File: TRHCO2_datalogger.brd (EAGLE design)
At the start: 57.7 x 51.3 mm, 31 parts, among them J3 USB-MICROB, U1 ATMEGA328P-MU, U7 SHT31/35, U8 MCP1703/3.3V, Y1 16MHZ

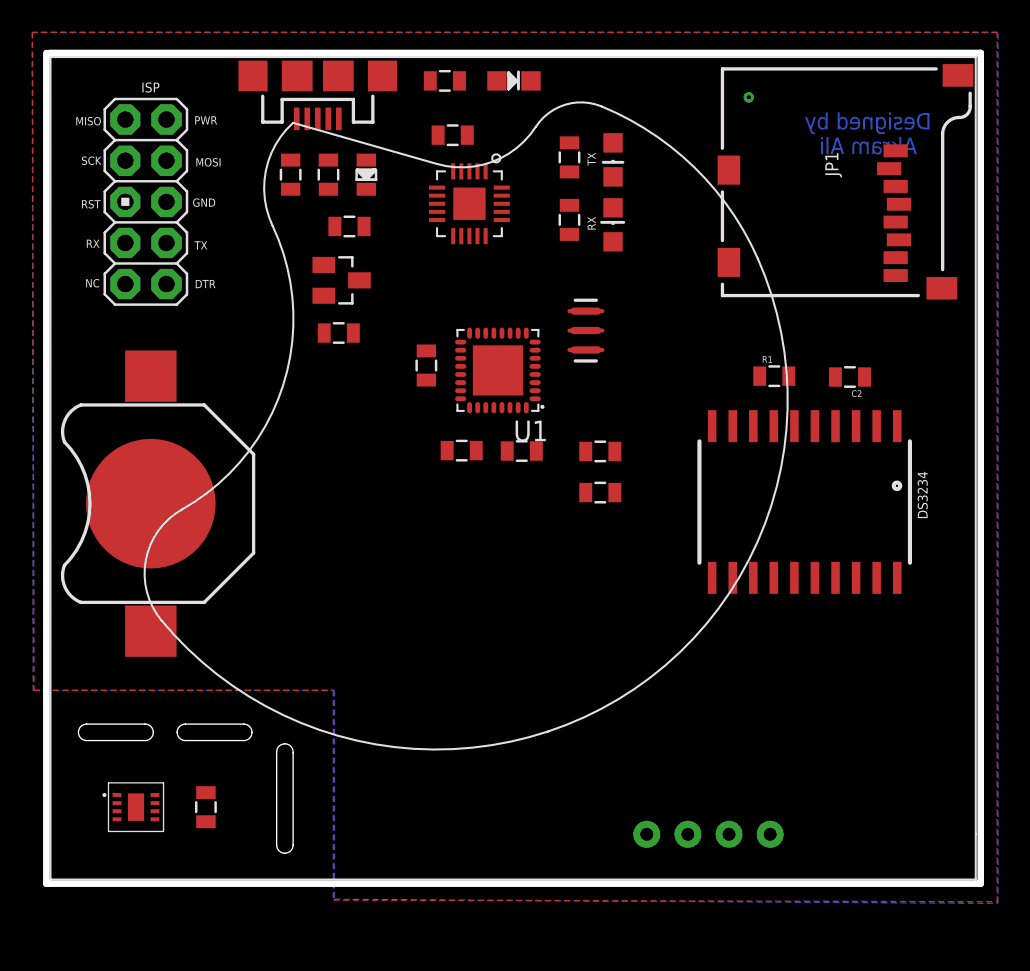
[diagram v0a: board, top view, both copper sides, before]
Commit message: Completed v0.1 design
Routed all traces
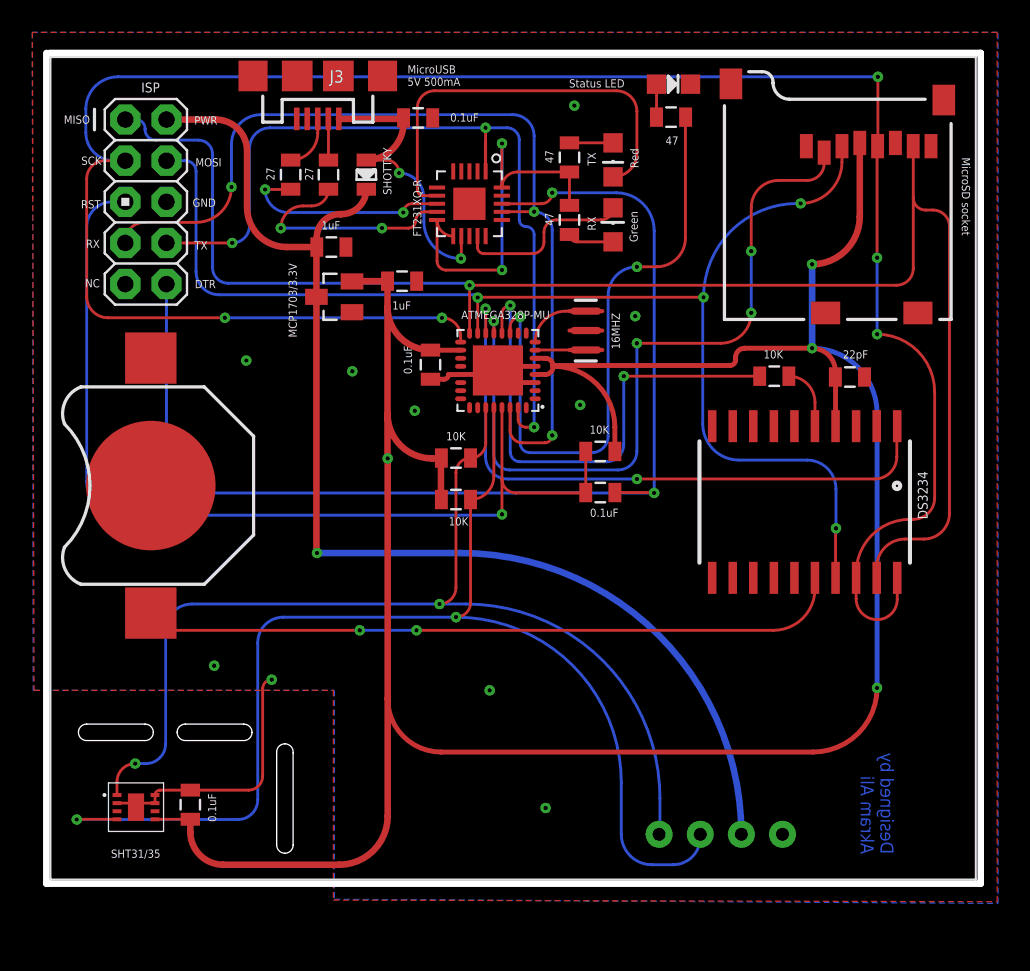
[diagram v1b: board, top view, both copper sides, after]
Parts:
- J3: value USB-MICROB -> MicroUSB (5V)
- JP1: value USD-SOCKETNEW -> MicroSD socket
- moved JP1 14.2 mm to (56.6, 38.0), turned to 0 degrees
- moved R4 14.1 mm to (39.3, 50.5), turned to 180 degrees
- moved LED1 9.86 mm to (39.4, 52.5)
- moved C6 5.05 mm to (22.7, 40.4)
- moved R6 5.05 mm to (26.0, 26.9), turned to 180 degrees
- moved C11 2.39 mm to (23.7, 50.4)
- moved C1 1.69 mm to (18.3, 42.5), turned to 0 degrees
- moved BAT1 1.12 mm to (7.16, 27.7)
- moved U8 1.11 mm to (18.5, 39.4), turned to 90 degrees
- moved C4 0.98 mm to (9.60, 8.03)
- moved R5 0.58 mm to (26.0, 29.4)
- moved C15 0.26 mm to (24.4, 35.2)
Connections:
- net D4 renamed N$2
- removed net N$1 (its old number): U1.12
- net D8: now also U1.12
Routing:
- net VCC: track 0.00 -> 166.4 mm, vias 0 -> 4
- net SCK: track 0.00 -> 129.7 mm, vias 0 -> 5
- net MISO: track 0.00 -> 95.3 mm, vias 0 -> 1
- net MOSI: track 0.00 -> 78.7 mm, vias 0 -> 4
- net SCL: track 0.00 -> 74.9 mm, vias 0 -> 2
- net PWR: track 0.00 -> 71.8 mm, vias 0 -> 1
- net DTR: track 0.00 -> 71.3 mm, vias 0 -> 2
- net SDA: track 0.00 -> 64.2 mm, vias 0 -> 2
- net RESET: track 0.00 -> 60.0 mm, vias 0 -> 1
- net RX: track 0.00 -> 56.1 mm, vias 0 -> 3
- net TX: track 0.00 -> 52.4 mm, vias 0 -> 3
- net D9: track 0.00 -> 46.0 mm, vias 0 -> 4
- net N$8: track 0.00 -> 44.3 mm, vias 0 -> 2
- net SS: track 0.00 -> 39.1 mm, vias 0 -> 2
- net N$1: track 0.00 -> 37.5 mm, vias 0 -> 2
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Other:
- board text added: "MicroUSB 5V 500mA"

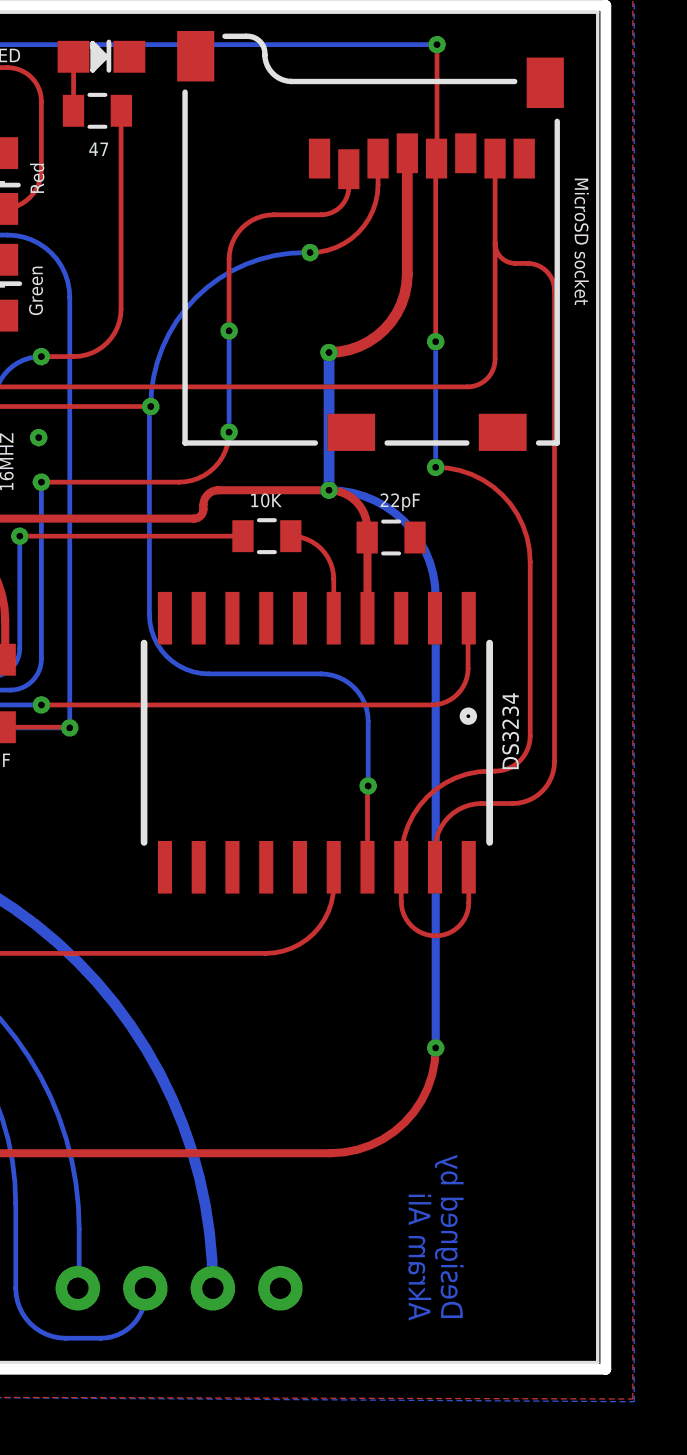
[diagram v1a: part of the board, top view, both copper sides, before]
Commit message: Added D battery input headers
Requires boost converter (https://www.sparkfun.com/products/10255) to allow 2 D batteries to supply at least 3V and get output 5V, 500mA
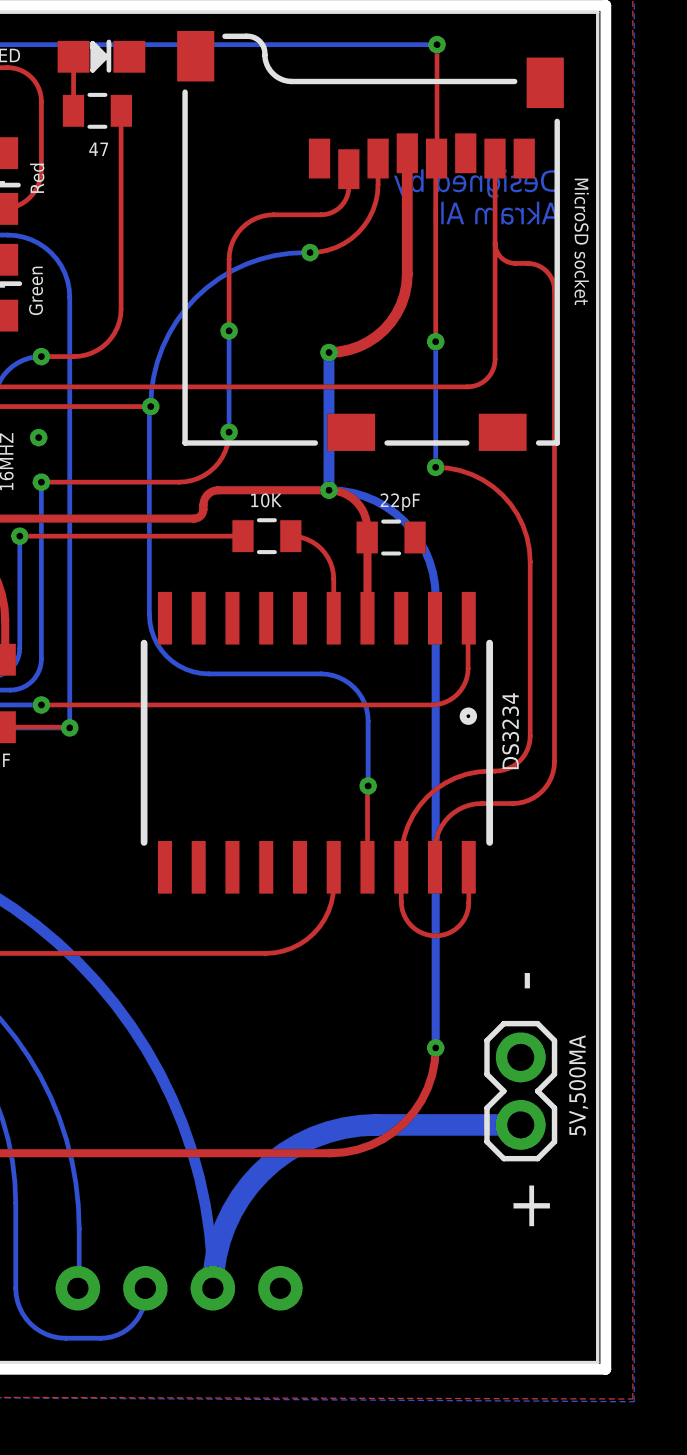
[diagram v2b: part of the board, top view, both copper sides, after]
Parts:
- added 5V,500MA: (no value), SparkFun-Connectors:1X02
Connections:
- net GND: now also 5V,500MA.1
- net PWR: now also 5V,500MA.2
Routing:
- net PWR: track 71.8 -> 85.9 mm
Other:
- board text added: "+"
- board text added: "-"
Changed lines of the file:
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@@
 <layers>
 <layer number="1" name="Top" color="4" fill="1" visible="yes" active="yes"/>
+<layer number="2" name="Route2" color="1" fill="3" visible="no" active="no"/>
+<layer number="3" name="Route3" color="4" fill="3" visible="no" active="no"/>
+<layer number="4" name="Route4" color="1" fill="4" visible="no" active="no"/>
+<layer number="5" name="Route5" color="4" fill="4" visible="no" active="no"/>
+<layer number="6" name="Route6" color="1" fill="8" visible="no" active="no"/>
+<layer number="7" name="Route7" color="4" fill="8" visible="no" active="no"/>
+<layer number="8" name="Route8" color="1" fill="2" visible="no" active="no"/>
+<layer number="9" name="Route9" color="4" fill="2" visible="no" active="no"/>
+<layer number="10" name="Route10" color="1" fill="7" visible="no" active="no"/>
+<layer number="11" name="Route11" color="4" fill="7" visible="no" active="no"/>
+<layer number="12" name="Route12" color="1" fill="5" visible="no" active="no"/>
+<layer number="13" name="Route13" color="4" fill="5" visible="no" active="no"/>
+<layer number="14" name="Route14" color="1" fill="6" visible="no" active="no"/>
+<layer number="15" name="Route15" color="4" fill="6" visible="no" active="no"/>
 <layer number="16" name="Bottom" color="1" fill="1" visible="yes" active="yes"/>
 <layer number="17" name="Pads" color="2" fill="1" visible="yes" active="yes"/>
@@
 <board>
 <plain>
-<text x="56.388" y="18.5166" size="0.8128" layer="122" font="vector" ratio="14" rot="MR270" align="center-left">T/RH/CO2 datalogger</text>
-<text x="51.0032" y="4.9784" size="0.8128" layer="16" font="vector" ratio="14" rot="SMR90">Designed by
+<text x="43.307" y="51.8668" size="0.8128" layer="122" font="vector" ratio="14" rot="MR180" align="center-left">T/RH/CO2 datalogger</text>
+<text x="56.6928" y="46.228" size="0.8128" layer="16" font="vector" ratio="14" rot="SMR0">Designed by
 Akram Ali
 </text>
-<text x="55.499" y="14.1986" size="0.508" layer="122" font="vector" rot="MR270">v0.1  |  January 2017</text>
+<text x="56.6674" y="50.419" size="0.508" layer="122" font="vector" rot="MR0">v0.1  |  January 2017</text>
 <text x="3.4036" y="50.5968" size="0.508" layer="121" font="vector" rot="R180">MISO</text>
 <text x="4.1148" y="48.0568" size="0.508" layer="121" font="vector" rot="R180">SCK</text>
@@
 <text x="23.0124" y="52.4256" size="0.508" layer="121" font="vector">MicroUSB
 5V 500mA</text>
+<text x="54.7116" y="8.5344" size="1.778" layer="121" font="vector">+</text>
+<text x="56.134" y="17.3736" size="1.778" layer="121" font="vector" rot="R90">-</text>
 </plain>
 <attributes>
@@
 <attribute name="VALUE" x="45.0088" y="35.5854" size="0.508" layer="121" font="vector"/>
 </element>
+<element name="5V,500MA" library="SparkFun-Connectors" package="1X02" value="" x="55.2196" y="14.8844" smashed="yes" rot="R270">
+<attribute name="NAME" x="57.0484" y="15.7226" size="0.6096" layer="121" font="vector" rot="R270"/>
+<attribute name="VALUE" x="52.0446" y="16.1544" size="1.27" layer="27" rot="R270"/>
+</element>
 </elements>
 <signals>
@@
 <via x="37.084" y="38.2016" extent="1-16" drill="0.254"/>
 <via x="23.4696" y="32.3596" extent="1-16" drill="0.254"/>
+<contactref element="5V,500MA" pad="1"/>
 </signal>
 <signal name="VCC">
@@
 <wire x1="17.4244" y1="23.5712" x2="26.2636" y2="23.5712" width="0.4064" layer="16"/>
 <wire x1="26.2636" y1="23.5712" x2="43.6372" y2="6.1976" width="0.4064" layer="16" curve="-90"/>
+<contactref element="5V,500MA" pad="2"/>
+<wire x1="55.2196" y1="12.3444" x2="49.784" y2="12.3444" width="0.8128" layer="16"/>
+<wire x1="49.784" y1="12.3444" x2="43.6372" y2="6.1976" width="0.8128" layer="16" curve="90"/>
 </signal>
 <signal name="MISO">

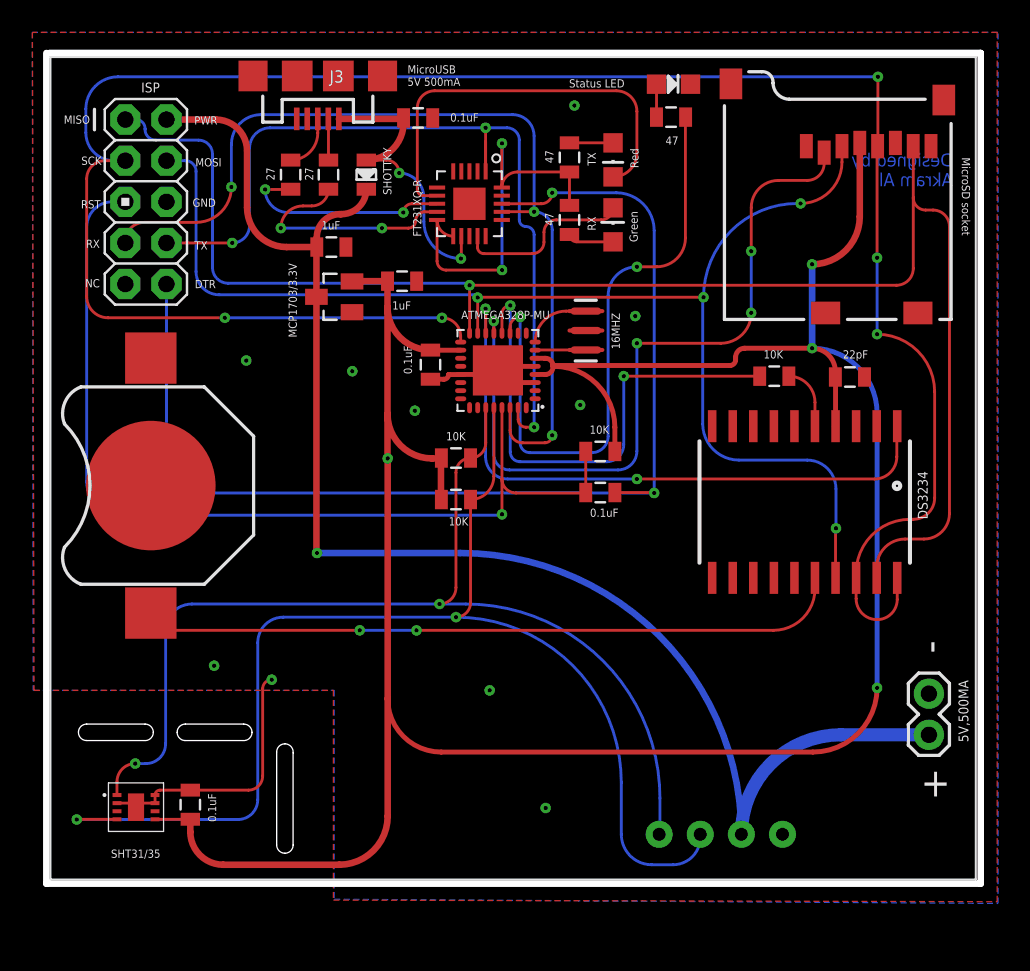
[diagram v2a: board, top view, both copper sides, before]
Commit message: Traces adjusted
Cleared some spacing between traces and vias
Added MPN for some components
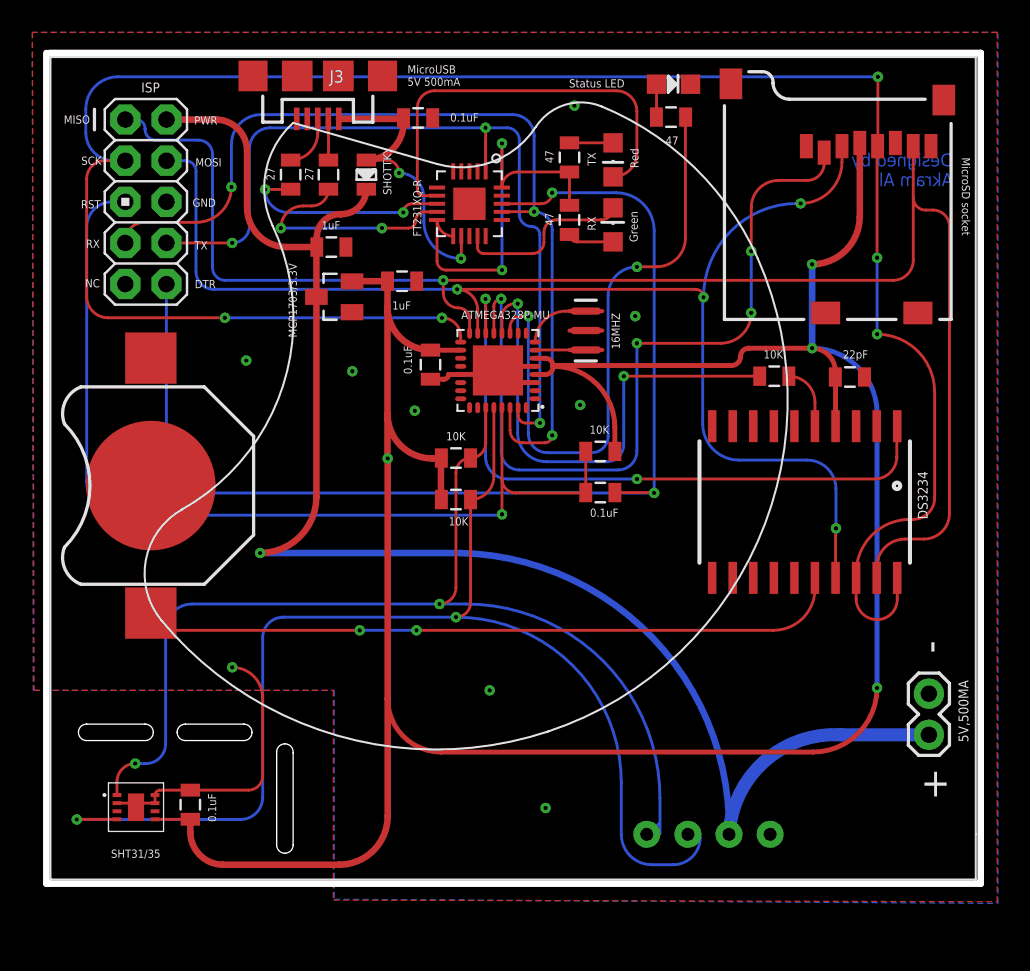
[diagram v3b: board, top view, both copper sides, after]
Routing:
- net PWR: track 85.9 -> 90.9 mm
- net D9: track 46.0 -> 48.4 mm
- net GND: track 26.1 -> 27.4 mm, vias 10 -> 9
- net MOSI: track 78.7 -> 80.0 mm
- net SS: track 39.1 -> 40.3 mm
- net SDA: track 64.2 -> 65.3 mm
- net D8: track 31.3 -> 30.6 mm
- net SCL: track 74.9 -> 75.5 mm
